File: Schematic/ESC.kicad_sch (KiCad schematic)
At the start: 0 parts

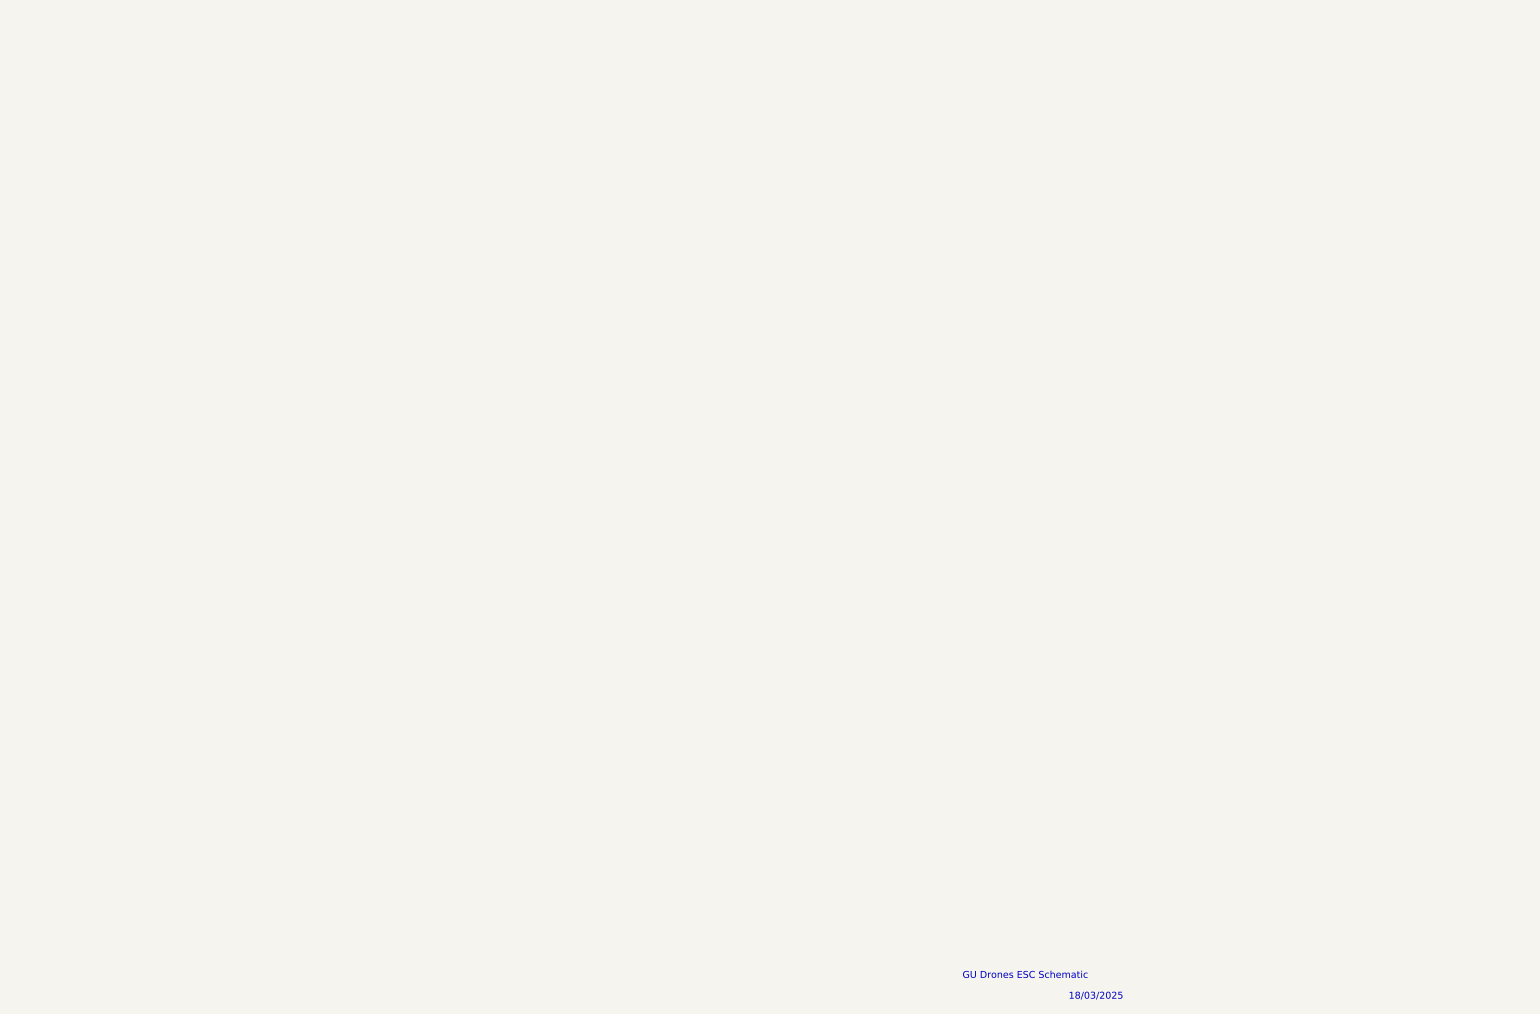
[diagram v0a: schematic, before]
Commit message: majority of schematic completed
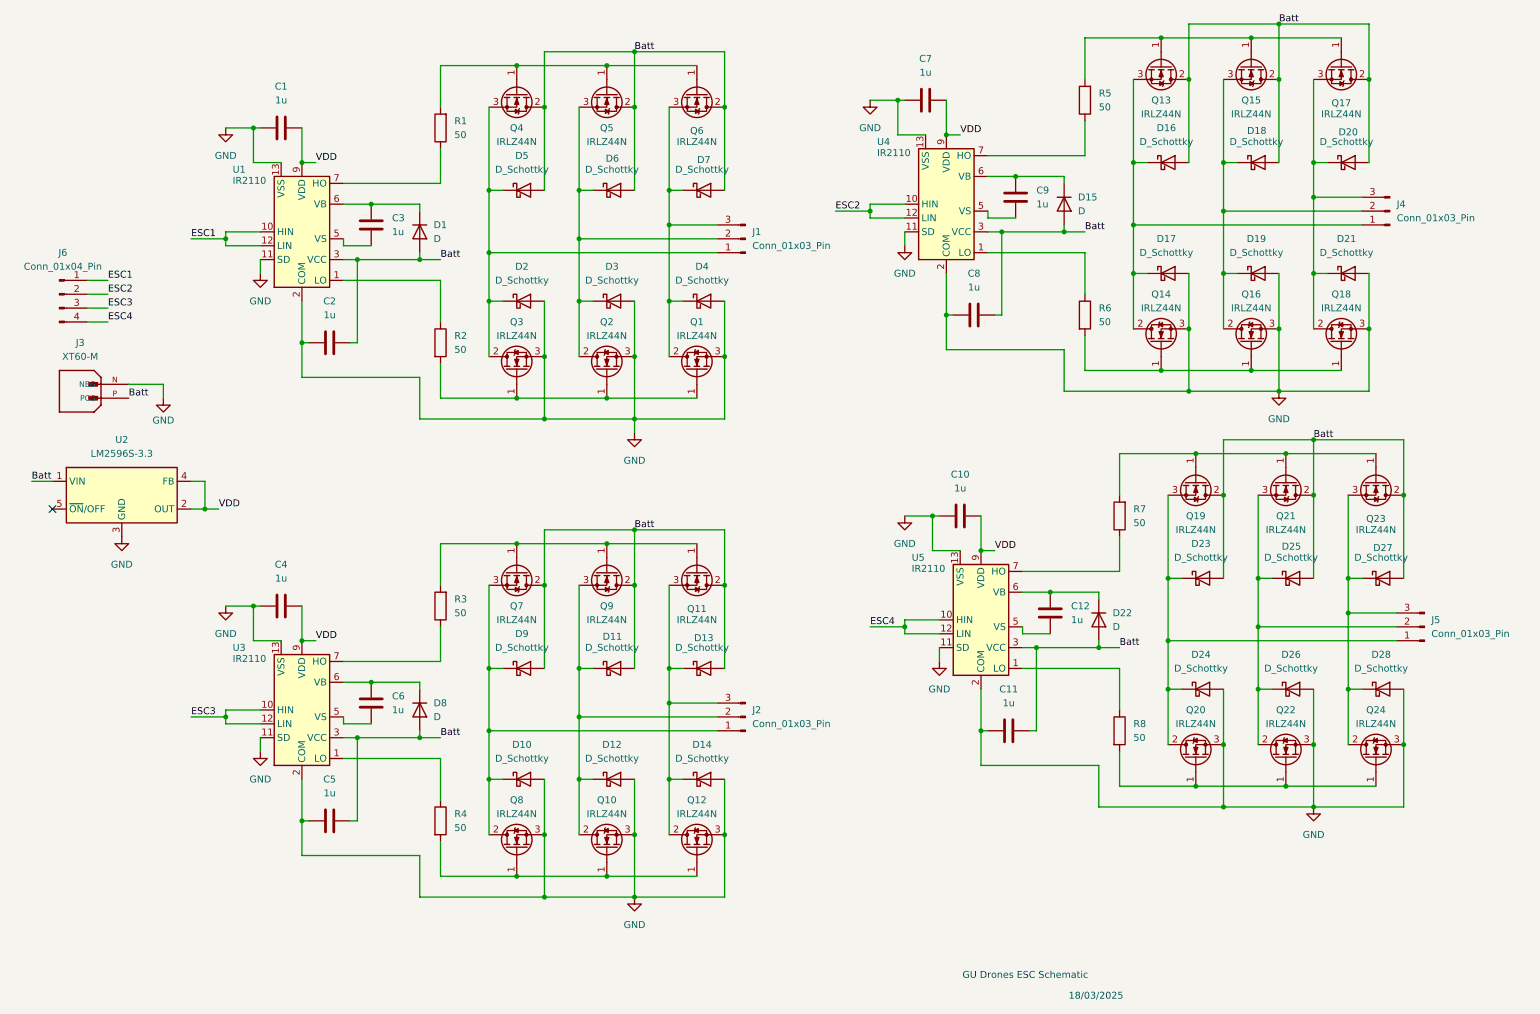
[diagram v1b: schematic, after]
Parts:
- added C1, C10, C11, C12, C2, C3, C4, C5, C6, C7, C8, C9: 1u, symbol Device:C
- added D1, D15, D22, D8: D, symbol Device:D
- added D10, D11, D12, D13, D14, D16, D17, D18, D19, D2, D20, D21, D23, D24, D25, D26, D27, D28, D3, D4, D5, D6, D7, D9: D_Schottky, symbol Device:D_Schottky
- added J1, J2, J4, J5: Conn_01x03_Pin, symbol Connector:Conn_01x03_Pin
- added J3: XT60-M, XT60-M:AMASS_XT60-M, symbol XT60:XT60-M
- added J6: Conn_01x04_Pin, symbol Connector:Conn_01x04_Pin
- added Q1, Q10, Q11, Q12, Q13, Q14, Q15, Q16, Q17, Q18, Q19, Q2, Q20, Q21, Q22, Q23, Q24, Q3, Q4, Q5, Q6, Q7, Q8, Q9: IRLZ44N, Package_TO_SOT_THT:TO-220-3_Vertical, symbol Transistor_FET:IRLZ44N
- added R1, R2, R3, R4, R5, R6, R7, R8: 50, symbol Device:R
- added U1, U3, U4, U5: IR2110, Package_DIP:DIP-14_W7.62mm, symbol Driver_FET:IR2110
- added U2: LM2596S-3.3, Package_TO_SOT_SMD:TO-263-5_TabPin3, symbol Regulator_Switching:LM2596S-3.3
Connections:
- new net: Q14.1 (G), Q16.1 (G), Q18.1 (G), R6.2
- new net: D16.1 (K), D17.1 (K), J4.1 (Pin_1), Q13.3 (S), Q14.2 (D)
- new net: D20.1 (K), D21.1 (K), J4.3 (Pin_3), Q17.3 (S), Q18.2 (D)
- new net: Q19.1 (G), Q21.1 (G), Q23.1 (G), R7.2
- new net: D23.1 (K), D24.1 (K), J5.1 (Pin_1), Q19.3 (S), Q20.2 (D)
- new net: Q10.1 (G), Q12.1 (G), Q8.1 (G), R4.2
- new net: D10.1 (K), D9.1 (K), J2.1 (Pin_1), Q7.3 (S), Q8.2 (D)
- new net: C9.1, U4.5 (VS)
- new net: C9.2, D15.1 (K), U4.6 (VB)
- new net: C6.2, D8.1 (K), U3.6 (VB)
- new net: D3.1 (K), D6.1 (K), J1.2 (Pin_2), Q2.2 (D), Q5.3 (S)
- new net: D11.1 (K), D12.1 (K), J2.2 (Pin_2), Q10.2 (D), Q9.3 (S)
- new net: D13.1 (K), D14.1 (K), J2.3 (Pin_3), Q11.3 (S), Q12.2 (D)
- new net: Q1.1 (G), Q2.1 (G), Q3.1 (G), R2.2
- new net: D2.1 (K), D5.1 (K), J1.1 (Pin_1), Q3.2 (D), Q4.3 (S)
- new net: Q20.1 (G), Q22.1 (G), Q24.1 (G), R8.2
- new net: D27.1 (K), D28.1 (K), J5.3 (Pin_3), Q23.3 (S), Q24.2 (D)
- new net: C12.1, U5.5 (VS)
- new net: C12.2, D22.1 (K), U5.6 (VB)
- new net: R8.1, U5.1 (LO)
- new net: Q11.1 (G), Q7.1 (G), Q9.1 (G), R3.2
- new net: R2.1, U1.1 (LO)
- new net: R3.1, U3.7 (HO)
- new net: D4.1 (K), D7.1 (K), J1.3 (Pin_3), Q1.2 (D), Q6.3 (S)
- new net: Q4.1 (G), Q5.1 (G), Q6.1 (G), R1.2
- new net: Q13.1 (G), Q15.1 (G), Q17.1 (G), R5.2
- new net: D18.1 (K), D19.1 (K), J4.2 (Pin_2), Q15.3 (S), Q16.2 (D)
- new net: R5.1, U4.7 (HO)
- new net: D25.1 (K), D26.1 (K), J5.2 (Pin_2), Q21.3 (S), Q22.2 (D)
- new net: R7.1, U5.7 (HO)
- new net: C3.1, U1.5 (VS)
- new net: C3.2, D1.1 (K), U1.6 (VB)
- new net: R1.1, U1.7 (HO)
- new net: R6.1, U4.1 (LO)
- new net: C6.1, U3.5 (VS)
- new net: R4.1, U3.1 (LO)
- new net Batt: C11.2, C2.2, C5.2, C8.2, D1.2 (A), D11.2 (A), D13.2 (A), D15.2 (A), D16.2 (A), D18.2 (A), D20.2 (A), D22.2 (A), D23.2 (A), D25.2 (A), D27.2 (A), D5.2 (A), D6.2 (A), D7.2 (A), D8.2 (A), D9.2 (A), J3.P (POS), Q11.2 (D), Q13.2 (D), Q15.2 (D), Q17.2 (D), Q19.2 (D), Q21.2 (D), Q23.2 (D), Q4.2 (D), Q5.2 (D), Q6.2 (D), Q7.2 (D), Q9.2 (D), U1.3 (VCC), U2.1 (VIN), U3.3 (VCC), U4.3 (VCC), U5.3 (VCC)
- new net ESC1: J6.1 (Pin_1), U1.10 (HIN), U1.12 (LIN)
- new net ESC2: J6.2 (Pin_2), U4.10 (HIN), U4.12 (LIN)
- new net ESC3: J6.3 (Pin_3), U3.10 (HIN), U3.12 (LIN)
- new net ESC4: J6.4 (Pin_4), U5.10 (HIN), U5.12 (LIN)
- new net GND: C1.1, C10.1, C11.1, C2.1, C4.1, C5.1, C7.1, C8.1, D10.2 (A), D12.2 (A), D14.2 (A), D17.2 (A), D19.2 (A), D2.2 (A), D21.2 (A), D24.2 (A), D26.2 (A), D28.2 (A), D3.2 (A), D4.2 (A), J3.N (NEG), Q1.3 (S), Q10.3 (S), Q12.3 (S), Q14.3 (S), Q16.3 (S), Q18.3 (S), Q2.3 (S), Q20.3 (S), Q22.3 (S), Q24.3 (S), Q3.3 (S), Q8.3 (S), U1.11 (SD), U1.13 (VSS), U1.2 (COM), U2.3 (GND), U3.11 (SD), U3.13 (VSS), U3.2 (COM), U4.11 (SD), U4.13 (VSS), U4.2 (COM), U5.11 (SD), U5.13 (VSS), U5.2 (COM)
- new net VDD: C1.2, C10.2, C4.2, C7.2, U1.9 (VDD), U2.2 (OUT), U2.4 (FB), U3.9 (VDD), U4.9 (VDD), U5.9 (VDD)
- no-connect marks 0 -> 1

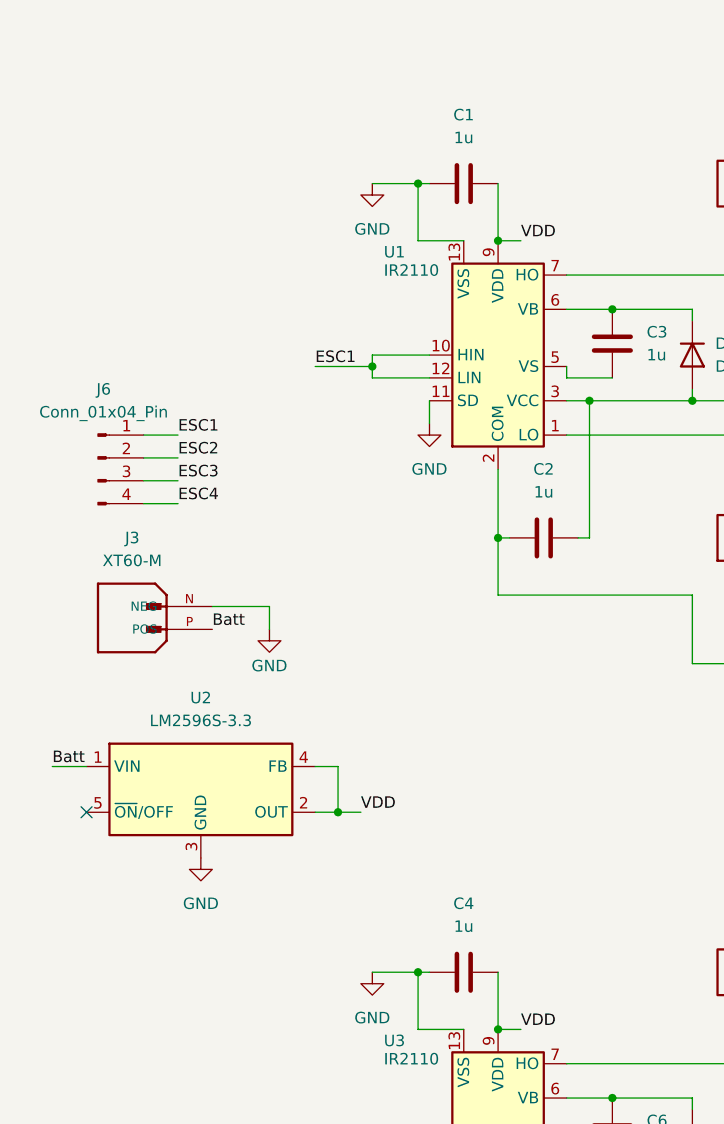
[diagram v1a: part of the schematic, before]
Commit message: Fixed voltage regulator
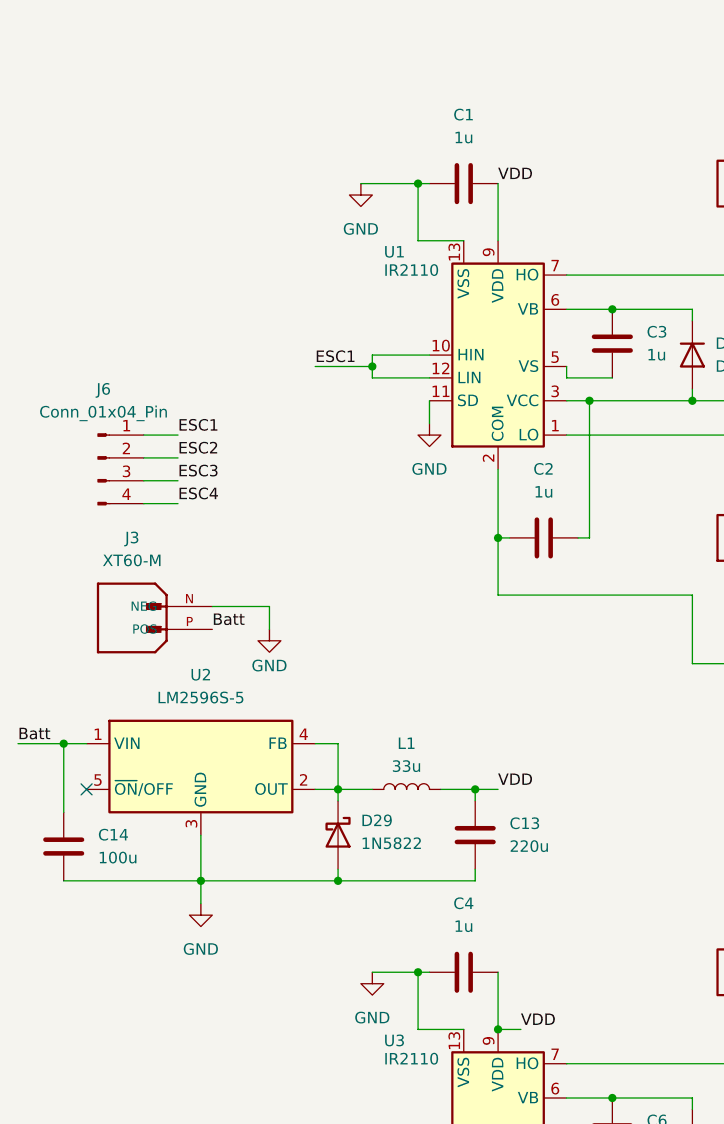
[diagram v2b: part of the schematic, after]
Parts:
- removed U2: LM2596S-3.3, Package_TO_SOT_SMD:TO-263-5_TabPin3, symbol Regulator_Switching:LM2596S-3.3
- added C13: 220u, symbol Device:C
- added C14: 100u, symbol Device:C
- added D29: 1N5822, Diode_THT:D_DO-201AD_P15.24mm_Horizontal, symbol Diode:1N5822
- added L1: 33u, symbol Device:L
- added U2: LM2596S-5, Package_TO_SOT_SMD:TO-263-5_TabPin3, symbol Regulator_Switching:LM2596S-5
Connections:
- net Batt: now also C14.1, U2.1 (VIN)
- net GND: now also C1.2, C13.2, C14.2, D29.2 (A), U2.3 (GND); no longer C1.1
- net VDD: now also C1.1, C13.1, L1.2; no longer C1.2
- new net: D29.1 (K), L1.1, U2.2 (OUT), U2.4 (FB)
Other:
- moved on the sheet: C1
